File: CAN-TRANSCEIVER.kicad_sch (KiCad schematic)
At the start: 16 parts, among them IC2 ATA6561-GAQW-N

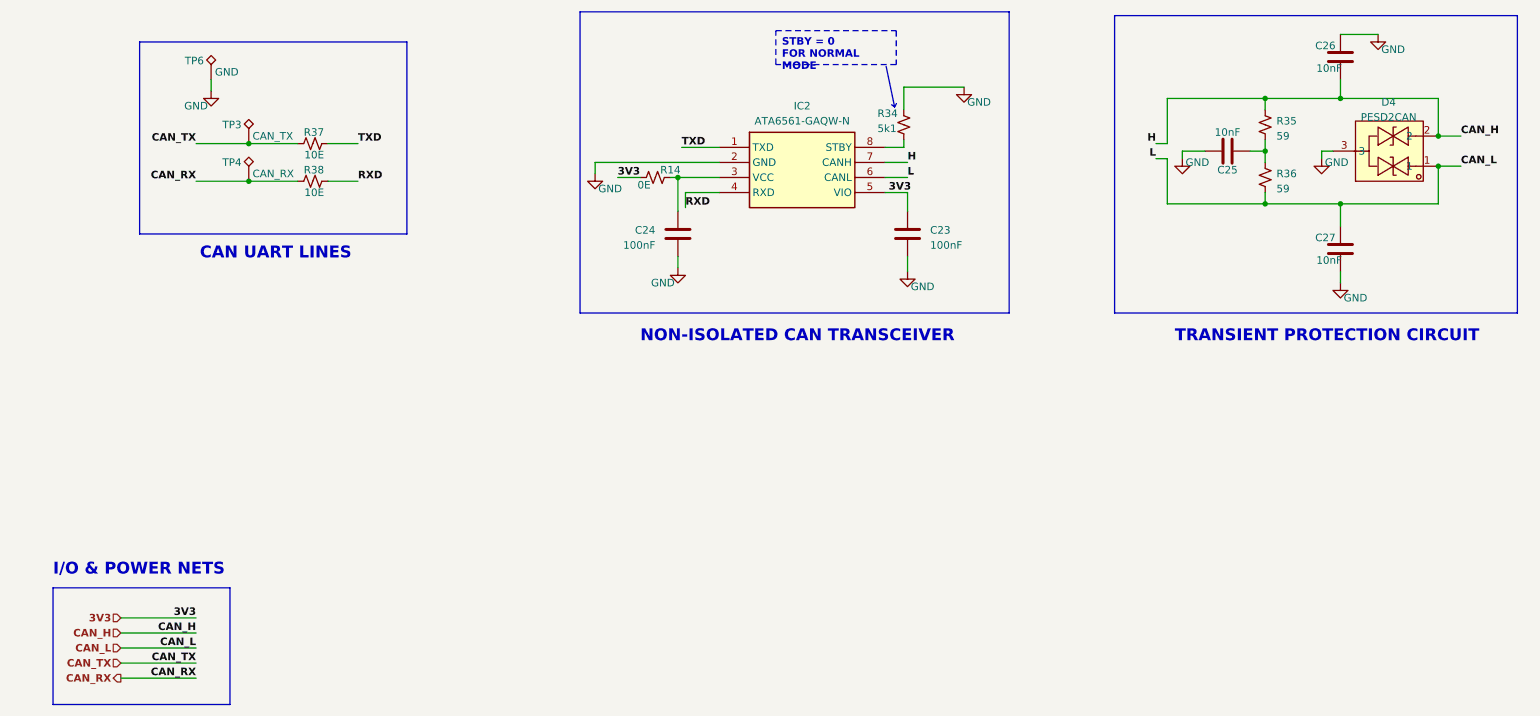
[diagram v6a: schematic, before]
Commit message: Corrected RS485 schematic
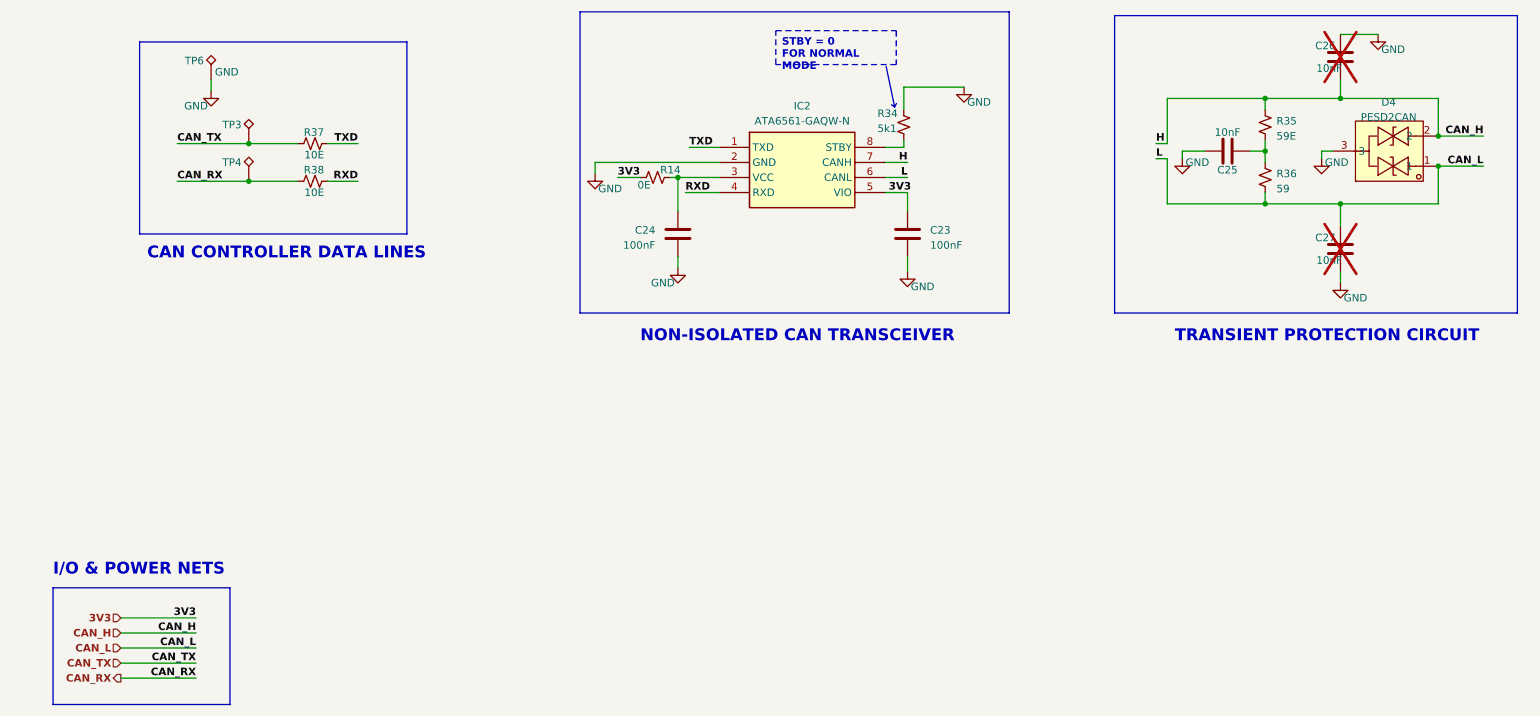
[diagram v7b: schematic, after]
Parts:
- C26, C27: now not fitted; now left out of the parts list
- R35: value 59 -> 59E
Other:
- note added: "CAN CONTROLLER DATA LINES"
- note removed: "CAN UART LINES"
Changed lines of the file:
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@@
     (stroke (width 1) (type default) (color 72 72 72 1))
   )
-  (wire (pts (xy 128.27 95.885) (xy 134.62 95.885))
+  (wire (pts (xy 129.54 95.885) (xy 134.62 95.885))
     (stroke (width 0) (type default))
   )
@@
     (stroke (width 0) (type default))
   )
-  (wire (pts (xy 255.905 93.98) (xy 259.715 93.98))
-    (stroke (width 0) (type default))
-  )
-  (wire (pts (xy 46.355 101.6) (xy 55.245 101.6))
+  (wire (pts (xy 255.905 93.98) (xy 263.525 93.98))
+    (stroke (width 0) (type default))
+  )
+  (wire (pts (xy 43.18 101.6) (xy 55.245 101.6))
     (stroke (width 0) (type default))
   )
@@
     (stroke (width 0) (type default))
   )
-  (wire (pts (xy 46.355 95.25) (xy 55.245 95.25))
+  (wire (pts (xy 43.18 95.25) (xy 55.245 95.25))
     (stroke (width 0) (type default))
   )
@@
     (stroke (width 1) (type default) (color 72 72 72 1))
   )
-  (wire (pts (xy 255.905 99.06) (xy 259.715 99.06))
+  (wire (pts (xy 255.905 99.06) (xy 263.525 99.06))
     (stroke (width 0) (type default))
   )
@@
   )
   (polyline (pts (xy 164.1856 89.0524) (xy 164.4904 88.4936))
-    (stroke (width 0) (type default))
-  )
-  (wire (pts (xy 128.905 106.045) (xy 128.905 103.505))
     (stroke (width 0) (type default))
   )
@@
     (effects (font (size 1.27 1.27) bold (color 0 0 255 1)) (justify left top))
   )
-  (text "CAN UART LINES" (at 46.99 114.935 0)
+  (text "CAN CONTROLLER DATA LINES" (at 38.1 114.935 0)
     (effects (font (size 2 2) bold (color 255 0 0 1)) (justify left bottom))
   )
@@
     (effects (font (size 2 2) bold (color 255 0 0 1)) (justify left bottom))
   )
-  (label "TXD" (at 73.66 95.25 0) (fields_autoplaced)
+  (label "TXD" (at 73.66 95.25 180) (fields_autoplaced)
+    (effects (font (size 1.27 1.27) bold (color 0 0 255 1)) (justify right bottom))
+  )
+  (label "CAN_RX" (at 43.18 101.6 0) (fields_autoplaced)
     (effects (font (size 1.27 1.27) bold (color 0 0 255 1)) (justify left bottom))
   )
-  (label "CAN_RX" (at 46.355 101.6 180) (fields_autoplaced)
-    (effects (font (size 1.27 1.27) bold (color 0 0 255 1)) (justify right bottom))
-  )
-  (label "L" (at 208.28 97.79 180) (fields_autoplaced)
+  (label "L" (at 208.28 97.79 0) (fields_autoplaced)
+    (effects (font (size 1.27 1.27) (thickness 0.254) bold (color 0 0 255 1)) (justify left bottom))
+  )
+  (label "H" (at 166.37 98.425 180) (fields_autoplaced)
     (effects (font (size 1.27 1.27) (thickness 0.254) bold (color 0 0 255 1)) (justify right bottom))
   )
-  (label "H" (at 166.37 98.425 0) (fields_autoplaced)
+  (label "H" (at 208.28 95.25 0) (fields_autoplaced)
     (effects (font (size 1.27 1.27) (thickness 0.254) bold (color 0 0 255 1)) (justify left bottom))
-  )
-  (label "H" (at 208.28 95.25 180) (fields_autoplaced)
-    (effects (font (size 1.27 1.27) (thickness 0.254) bold (color 0 0 255 1)) (justify right bottom))
   )
   (label "CAN_H" (at 46.355 177.8 180) (fields_autoplaced)
@@
     (effects (font (size 1.27 1.27) bold (color 0 0 255 1)) (justify right bottom))
   )
-  (label "CAN_L" (at 259.715 99.06 0) (fields_autoplaced)
-    (effects (font (size 1.27 1.27) bold (color 0 0 0 1)) (justify left bottom))
+  (label "CAN_L" (at 263.525 99.06 180) (fields_autoplaced)
+    (effects (font (size 1.27 1.27) bold (color 0 0 0 1)) (justify right bottom))
   )
   (label "3V3" (at 163.195 103.505 0) (fields_autoplaced)
@@
     (effects (font (size 1.27 1.27) bold (color 0 0 255 1)) (justify right bottom))
   )
-  (label "RXD" (at 73.66 101.6 0) (fields_autoplaced)
+  (label "RXD" (at 73.66 101.6 180) (fields_autoplaced)
+    (effects (font (size 1.27 1.27) bold (color 0 0 255 1)) (justify right bottom))
+  )
+  (label "TXD" (at 129.54 95.885 0) (fields_autoplaced)
     (effects (font (size 1.27 1.27) bold (color 0 0 255 1)) (justify left bottom))
   )
-  (label "TXD" (at 128.27 95.885 0) (fields_autoplaced)
-    (effects (font (size 1.27 1.27) bold (color 0 0 255 1)) (justify left bottom))
-  )
-  (label "CAN_H" (at 259.715 93.98 0) (fields_autoplaced)
-    (effects (font (size 1.27 1.27) bold (color 0 0 0 1)) (justify left bottom))
-  )
-  (label "RXD" (at 128.905 106.045 0) (fields_autoplaced)
+  (label "CAN_H" (at 263.525 93.98 180) (fields_autoplaced)
+    (effects (font (size 1.27 1.27) bold (color 0 0 0 1)) (justify right bottom))
+  )
+  (label "RXD" (at 128.905 103.505 0) (fields_autoplaced)
     (effects (font (size 1.27 1.27) bold (color 0 0 255 1)) (justify left bottom))
   )
@@
     (effects (font (size 1.27 1.27) bold (color 255 0 0 1)) (justify left bottom))
   )
-  (label "L" (at 166.37 100.965 0) (fields_autoplaced)
-    (effects (font (size 1.27 1.27) (thickness 0.254) bold (color 0 0 255 1)) (justify left bottom))
-  )
-  (label "CAN_TX" (at 46.355 95.25 180) (fields_autoplaced)
-    (effects (font (size 1.27 1.27) bold (color 0 0 255 1)) (justify right bottom))
+  (label "L" (at 166.37 100.965 180) (fields_autoplaced)
+    (effects (font (size 1.27 1.27) (thickness 0.254) bold (color 0 0 255 1)) (justify right bottom))
+  )
+  (label "CAN_TX" (at 43.18 95.25 0) (fields_autoplaced)
+    (effects (font (size 1.27 1.27) bold (color 0 0 255 1)) (justify left bottom))
   )
   (hierarchical_label "CAN_L" (shape input) (at 33.655 180.34 180) (fields_autoplaced)
@@
     )
     (property "Value" "CAN_RX" (at 55.88 100.33 0)
-      (effects (font (size 1.27 1.27)) (justify left))
+      (effects (font (size 1.27 1.27)) (justify left) hide)
     )
     (property "Footprint" "ESP32-S3_Dev_Board:Test_Pad_1.5mm" (at 60.325 101.6 0)
@@
   )
   (symbol (lib_id "ESP32-S3_DB:C") (at 239.395 80.645 180) (unit 1)
-    (in_bom yes) (on_board yes) (dnp no)
+    (in_bom no) (on_board yes) (dnp yes)
     (property "Reference" "C26" (at 236.855 78.74 0)
       (effects (font (size 1.27 1.27)))
@@
     )
     (property "Value" "CAN_TX" (at 55.88 93.98 0)
-      (effects (font (size 1.27 1.27)) (justify left))
+      (effects (font (size 1.27 1.27)) (justify left) hide)
     )
     (property "Footprint" "ESP32-S3_Dev_Board:Test_Pad_1.5mm" (at 60.325 95.25 0)
@@
       (effects (font (size 1.27 1.27)) (justify right))
     )
-    (property "Value" "59" (at 228.6 93.98 0)
+    (property "Value" "59E" (at 228.6 93.98 0)
       (effects (font (size 1.27 1.27)) (justify right))
     )
@@
   )
   (symbol (lib_id "ESP32-S3_DB:C") (at 239.395 113.03 180) (unit 1)
-    (in_bom yes) (on_board yes) (dnp no)
+    (in_bom no) (on_board yes) (dnp yes)
     (property "Reference" "C27" (at 236.855 111.125 0)
       (effects (font (size 1.27 1.27)))

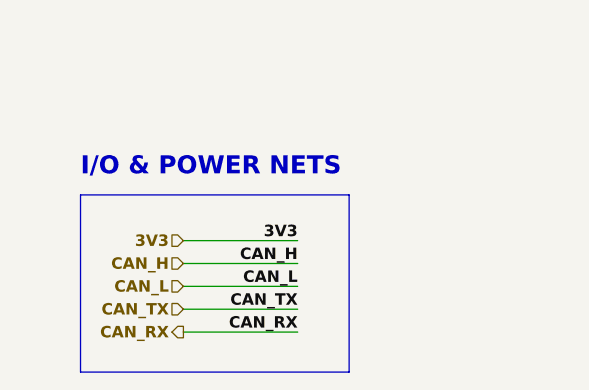
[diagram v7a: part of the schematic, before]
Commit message: Added CAN Jumpers, changed jumper pitch to 1.27mm
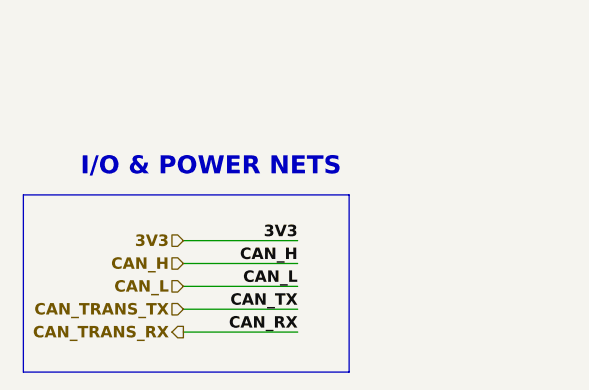
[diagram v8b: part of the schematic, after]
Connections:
- net CAN_RX renamed CAN_TRANS_RX
- net CAN_TX renamed CAN_TRANS_TX
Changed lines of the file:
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@@
     (stroke (width 0) (type default))
   )
-  (bus (pts (xy 52.07 189.865) (xy 22.225 189.865))
+  (bus (pts (xy 52.07 189.865) (xy 15.875 189.865))
     (stroke (width 1) (type default) (color 72 72 72 1))
   )
@@
     (stroke (width 1) (type default) (color 72 72 72 1))
   )
-  (bus (pts (xy 22.225 189.865) (xy 22.225 170.18))
+  (bus (pts (xy 15.875 189.865) (xy 15.875 170.18))
     (stroke (width 1) (type default) (color 72 72 72 1))
   )
@@
     (stroke (width 0) (type default))
   )
-  (bus (pts (xy 22.225 170.18) (xy 52.07 170.18))
+  (bus (pts (xy 15.875 170.18) (xy 52.07 170.18))
     (stroke (width 1) (type default) (color 72 72 72 1))
   )
@@
     (effects (font (size 1.27 1.27) bold (color 0 0 0 1)) (justify right))
   )
-  (hierarchical_label "CAN_TX" (shape input) (at 33.655 182.88 180) (fields_autoplaced)
+  (hierarchical_label "CAN_TRANS_TX" (shape input) (at 33.655 182.88 180) (fields_autoplaced)
     (effects (font (size 1.27 1.27) bold (color 0 0 255 1)) (justify right))
   )
@@
     (effects (font (size 1.27 1.27) bold (color 0 0 0 1)) (justify right))
   )
-  (hierarchical_label "CAN_RX" (shape output) (at 33.655 185.42 180) (fields_autoplaced)
+  (hierarchical_label "CAN_TRANS_RX" (shape output) (at 33.655 185.42 180) (fields_autoplaced)
     (effects (font (size 1.27 1.27) bold (color 0 0 255 1)) (justify right))
   )
